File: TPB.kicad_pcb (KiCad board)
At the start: 2 copper layers, 100 x 100 mm, 17 parts, among them J200 09031967921, J400 XT60PW-M, U401 XL4015

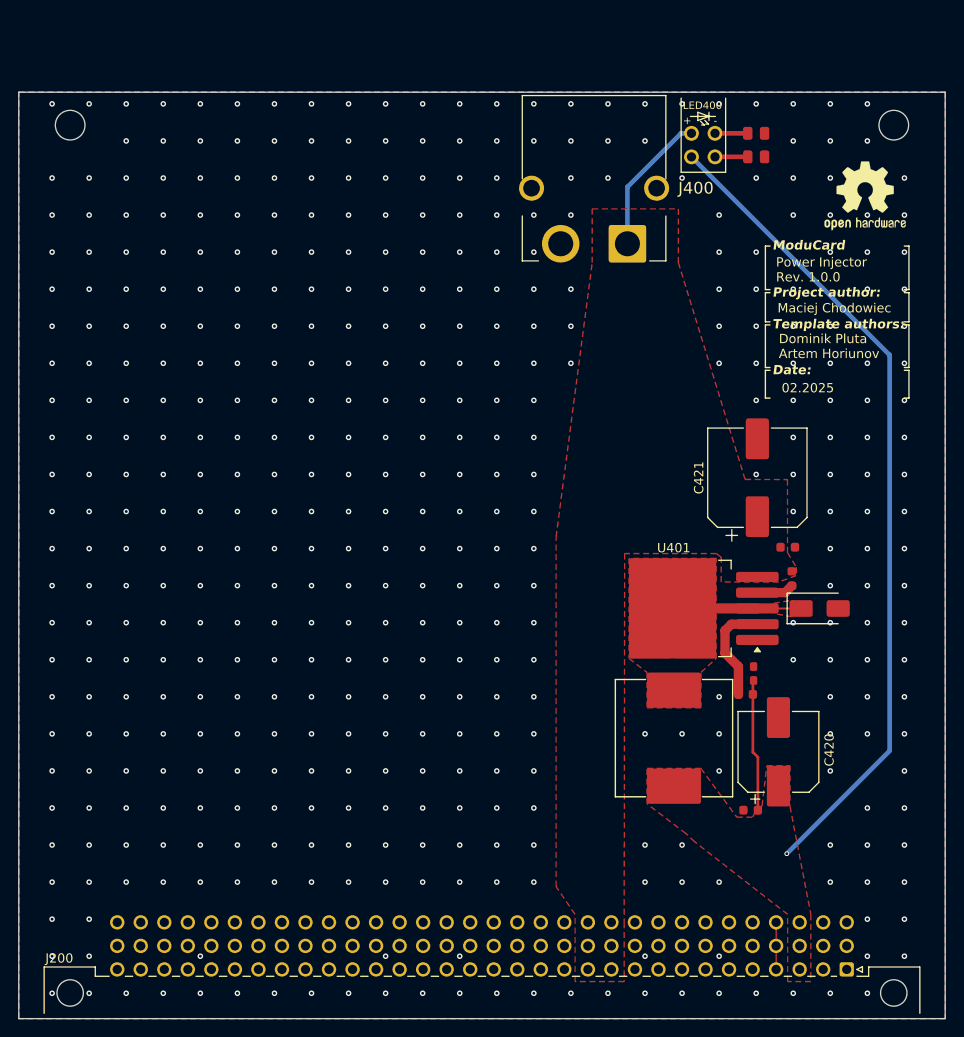
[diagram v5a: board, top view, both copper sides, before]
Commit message: add LED list on back
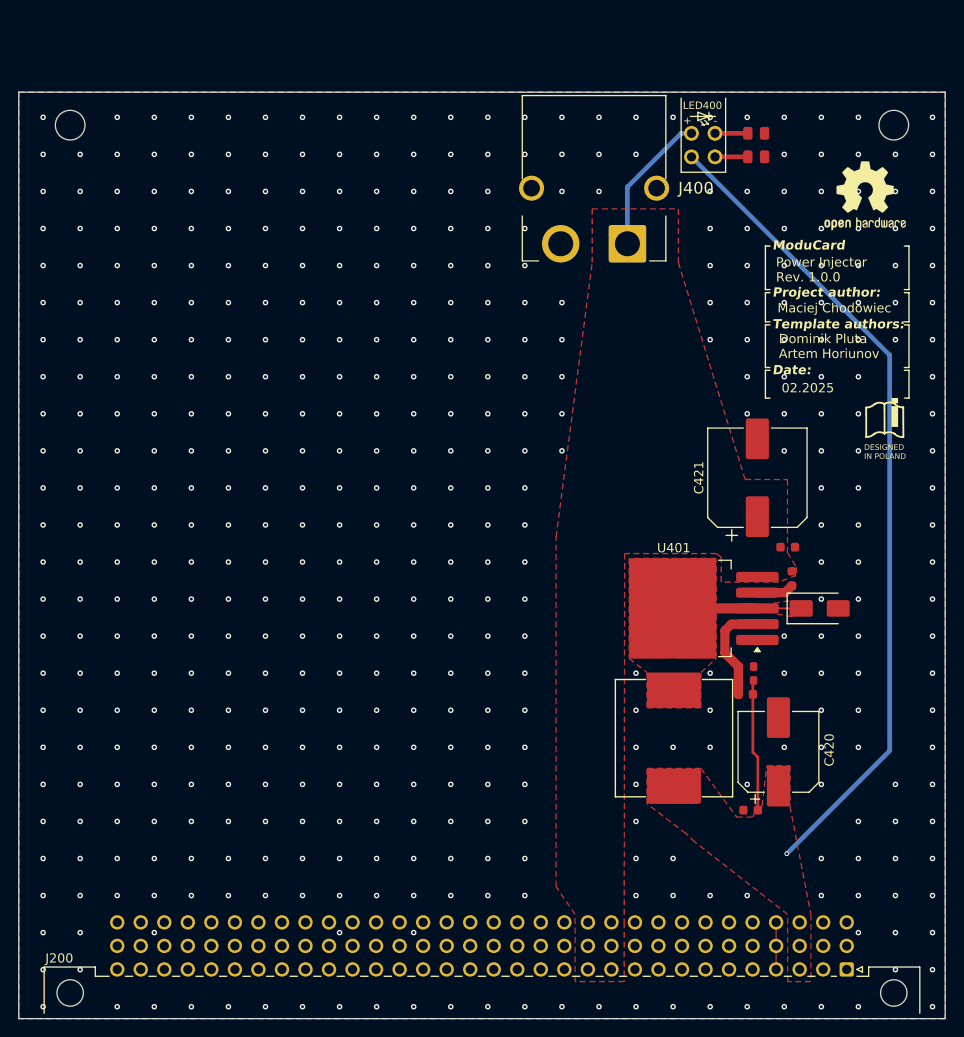
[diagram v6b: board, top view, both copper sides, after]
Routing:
- net GND: vias 452 -> 472
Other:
- board text added: "DESIGNED IN POLAND"
- board text added: "RED: +12V YELLOW: +5V STDBY"
- board text added: "i"

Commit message: add Gerger
add Gerger, add jlc number
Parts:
- added REF**: Part_Num_JLCPCB, PCM_JLCPCB:Part_Num_JLCPCB, F.Cu at (54.4, 148.3)
